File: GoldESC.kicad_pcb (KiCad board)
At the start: 4 copper layers, 98 x 40 mm, 153 parts, among them J1 PhaseOut, J10 Conn_01x06, J2 PhaseOut, J3 PhaseOut, J30 CanOut, J40 Supply, J81 Conn_02x07_Counter_Clockwise, J82 Conn_01x06, Q1 YJG150N03A, Q2 YJG150N03A, Q3 YJG150N03A, Q4 YJG150N03A, Q5 YJG150N03A, Q6 YJG150N03A, U2 DRV8300NIPWR, U30 MCP2551-I-SN, U31 CPDT-12V, U4 INA185A1, U5 INA185A1, U50 SY8113BADC, U6 INA185A1, U60 SY8113BADC, U80 STM32F103C8Tx, U81 Crystal_GND3

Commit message: major schematic and pcb changes for production ready prototype
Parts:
- removed ? (x3): , 
- removed C85: 2.2uF, Capacitor_SMD:C_0603_1608Metric
- removed D74, D75, D76, D77: Z3V3, Diode_SMD:D_MiniMELF
- removed D80, D81: LED_Dual_AKA, LED_THT:LED_D3.0mm-3
- removed J10: Conn_01x06, Connector_PinSocket_2.54mm:PinSocket_1x06_P2.54mm_Vertical
- removed L30: KCZ1210, AlfredoFootprints:KCZ1210
- removed R33: 120R?, Resistor_THT:R_Axial_DIN0207_L6.3mm_D2.5mm_P10.16mm_Horizontal
- removed R5, R6, R8, R9: 1K, Resistor_SMD:R_0603_1608Metric
- removed R77: 2K2, Resistor_SMD:R_0603_1608Metric
- removed TP1, TP10, TP11, TP12, TP13, TP14, TP15, TP2, TP3, TP30, TP31, TP32, TP33, TP4, TP40, TP41, TP5, TP50, TP6, TP7, TP8, TP81, TP9: TestPoint, AlfredoFootprints:GE_TestPoint_Loop
- removed the U50 at (175.4, 86.1)
- added C41: 330uF, AlfredoFootprints:Cap_THT_LowESR_330uF, B.Cu at (4.06, -4.19)
- added D82: LED_Green, LED_SMD:LED_0805_2012Metric, F.Cu at (6.60, 7.80)
- added D83: LED_Red, LED_SMD:LED_0805_2012Metric, F.Cu at (6.60, 6.20)
- added D84: LED_Green, LED_SMD:LED_0805_2012Metric, F.Cu at (6.60, -6.20)
- added D85: LED_Red, LED_SMD:LED_0805_2012Metric, F.Cu at (6.60, -7.80)
- added J4: GND, AlfredoFootprints:GE_PwrPad1, F.Cu at (22.2, 3.50)
- added J41: Gnd, AlfredoFootprints:GE_PwrPad1, F.Cu at (-0.45, -7.00)
- added J5: DB15_Female_HighDensity, Connector_Dsub:DSUB-15-HD_Female_Horizontal_P2.29x1.98mm_EdgePinOffset3.03mm_Housed_MountingHolesOffset4.94mm, F.Cu at (-130.5, -12.1)
- added REF**: MountingHole_2.2mm_M2, MountingHole:MountingHole_2.2mm_M2, F.Cu at (-23.4, 3.70)
- added REF**: MountingHole_2.2mm_M2, MountingHole:MountingHole_2.2mm_M2, F.Cu at (26.8, -3.43)
- added TP60: TestPoint, AlfredoFootprints:GE_TestPoint_Loop, F.Cu at (5.10, 14.3)
- added U50: SY8113BADC, Package_TO_SOT_SMD:TSOT-23-6, F.Cu at (-123.1, 34.7)
- added U50: SPX3819M5-L-3-3, Package_TO_SOT_SMD:SOT-23-5, F.Cu at (1.15, 15.2)
- C1, C2, C3: value 10uF,25V -> 2.2uF,50V; footprint Capacitor_SMD:C_0805_2012Metric -> Capacitor_SMD:C_1206_3216Metric
- C4, C42, C5, C50, C51, C52, C53, C6, C60, C61, C62, C63, C7, C8, C81, C82, C83, C84, C9: footprint Capacitor_SMD:C_0603_1608Metric -> Capacitor_SMD:C_0402_1005Metric
- C40: footprint AlfredoFootprints:TGD_lowESR_cap -> AlfredoFootprints:Cap_THT_LowESR_330uF; moved to B.Cu
- C80, C88, C89: footprint Capacitor_SMD:C_0603_1608Metric -> Capacitor_SMD:C_0402_1005Metric; moved to B.Cu
- D1, D2, D3, D42: value ZMM3V3 -> B3V3; footprint Diode_SMD:D_MiniMELF -> Diode_SMD:D_SOD-323_HandSoldering
- D4, D5, D6: value CRH01 -> 1N58; footprint Diode_SMD:D_SOD-123F -> Diode_SMD:D_SOD-323_HandSoldering
- D40, D41: value B5819W -> 1N58; footprint Diode_SMD:D_SOD-123 -> Diode_SMD:D_SOD-323_HandSoldering
- D70, D71, D72, D73: value Z3V3 -> SM05T1G; footprint Diode_SMD:D_MiniMELF -> Package_TO_SOT_SMD:SOT-23; moved to B.Cu
- G***: moved to F.Cu
- J1, J2, J3: footprint AlfredoFootprints:TGD_ESC_PwrPad -> AlfredoFootprints:GE_PwrPad1
- J40: value Supply -> Vin; footprint TerminalBlock:TerminalBlock_bornier-2_P5.08mm -> AlfredoFootprints:GE_PwrPad1
- J81: footprint Connector_IDC:IDC-Header_2x07_P2.54mm_Vertical -> AlfredoFootprints:Connector_2x05_P1.27mm_IDC
- J82: value Conn_01x06 -> Conn_01x04; footprint Connector_PinSocket_2.54mm:PinSocket_1x06_P2.54mm_Vertical -> AlfredoFootprints:Connector_1x04_P1.27mm_SwdProg
- Q1, Q2, Q3, U30, U31: moved to B.Cu
- R10, R11, R12, R13, R14, R15, R16, R17, R18, R19, R20, R21, R22, R23, R24, R40, R42, R43, R50, R51, R60, R61, R70, R71, R72, R73, R74, R75, R76, R80: footprint Resistor_SMD:R_0603_1608Metric -> Resistor_SMD:R_0402_1005Metric
- R30, R31, R4, R7, R81, R82, R83, R84, R85, R86: footprint Resistor_SMD:R_0603_1608Metric -> Resistor_SMD:R_0402_1005Metric; moved to B.Cu
- R32: value 50K? -> 50K; footprint Resistor_THT:R_Axial_DIN0207_L6.3mm_D2.5mm_P10.16mm_Horizontal -> Resistor_SMD:R_0402_1005Metric; moved to B.Cu
- R41: value 10K RTC -> 10K NTC; footprint Resistor_SMD:R_0603_1608Metric -> Resistor_SMD:R_0402_1005Metric
- U80: value STM32F103C8Tx -> STM32F103CBTx
- U81: value Crystal_GND3 -> ABM3B-8.000MHZ; moved to B.Cu
- moved R50 307.4 mm to (-123.7, 38.2), turned to 0 degrees
- moved R51 301.3 mm to (-118.1, 32.3), turned to 0 degrees
- moved R60 301.1 mm to (-114.1, 30.3), turned to 0 degrees
- moved U60 300.6 mm to (-117.5, 26.3), turned to 0 degrees
- moved C62 300.4 mm to (-118.5, 34.8), turned to 0 degrees
- moved L60 300.4 mm to (-122.9, 30.4), turned to 0 degrees
- moved D41 300.0 mm to (-114.0, 37.5)
- moved L50 299.4 mm to (-122.9, 26.1), turned to 0 degrees
- moved C52 299.4 mm to (-118.1, 29.8), turned to 0 degrees
- moved C61 297.5 mm to (-119.7, 38.2), turned to 0 degrees
- moved R61 294.9 mm to (-108.9, 27.8), turned to 0 degrees
- moved C60 294.8 mm to (-108.9, 25.3), turned to 0 degrees
- moved C63 293.8 mm to (-114.1, 32.8), turned to 0 degrees
- moved C53 292.0 mm to (-112.9, 27.8), turned to 0 degrees
- moved C51 291.9 mm to (-112.9, 25.3), turned to 0 degrees
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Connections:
- D70 pad 2: GND -> QuadA
- D71 pad 1: QuadA -> LimitA
- D71 pad 2: GND -> LimitB
- D72 pad 1: Limit2C -> LimitC
- D72 pad 2: GND -> LimitD
- D73 pad 1: Limit2A -> LimitE
- D73 pad 2: GND -> unconnected-(D73-Pad2)
- J40 pad 1: GND -> VDD
- J81 pad 1: +5V -> +3V3
- J81 pad 10: Limit1B -> LimitD
- J81 pad 2: QuadA -> +5V
- J81 pad 3: +3V3 -> GND
- J81 pad 4: QuadB -> LimitA
- J81 pad 5: GND -> QuadB_USBDM
- J81 pad 6: USB_DP -> LimitB
- J81 pad 7: GND -> QuadA_USBDP
- J81 pad 8: USB_DM -> LimitC
- J81 pad 9: Limit1C -> LimitE
- R4 pad 2: Net-(R4-Pad2) -> /GE-Fets-A/REF_1V65
- R7 pad 1: Net-(R4-Pad2) -> /GE-Fets-A/REF_1V65
- R72 pad 1: Limit2C -> LimitA
- R73 pad 1: Limit2A -> LimitB
- R74 pad 1: Limit1C -> LimitC
- R75 pad 1: Limit1A -> LimitD
- R76 pad 1: Limit1B -> LimitE
- R81 pad 2: USB_DM -> QuadB_USBDM
- R82 pad 2: USB_DP -> QuadA_USBDP
- U30 pad 6: Net-(L30-Pad2) -> CAN_L
- U30 pad 7: Net-(L30-Pad1) -> CAN_H
- U4 pad 5: Net-(R4-Pad2) -> /GE-Fets-A/REF_1V65
- U5 pad 5: Net-(R5-Pad2) -> /GE-Fets-A/REF_1V65
- U6 pad 5: Net-(R6-Pad2) -> /GE-Fets-A/REF_1V65
- U80 pad 17: QuadA -> unconnected-(U80-Pad17)
- U80 pad 19: QuadB -> unconnected-(U80-Pad19)
- U80 pad 38: Limit2C -> unconnected-(U80-Pad38)
- U80 pad 39: Limit1A -> LimitA
- U80 pad 40: Limit1B -> LimitB
- U80 pad 41: Limit1C -> LimitC
- U80 pad 42: Limit2A -> LimitD
- U80 pad 43: Limit2B -> LimitE
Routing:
- net VDD: track 158.0 -> 0.00 mm
- net GND: track 156.2 -> 0.00 mm, vias 41 -> 0
- net +5V: track 103.0 -> 0.00 mm, vias 6 -> 0
- net sVLT_B: track 95.8 -> 0.00 mm, vias 1 -> 0
- net sCUR_A: track 92.7 -> 0.00 mm, vias 1 -> 0
- net sCUR_B: track 92.5 -> 0.00 mm, vias 1 -> 0
- net sVLT_C: track 92.5 -> 0.00 mm, vias 1 -> 0
- net sVLT_A: track 88.8 -> 0.00 mm, vias 1 -> 0
- net sVLT_VDD: track 87.4 -> 0.00 mm, vias 1 -> 0
- net sCUR_C: track 87.3 -> 0.00 mm, vias 1 -> 0
- net INLC: track 67.2 -> 0.00 mm, vias 2 -> 0
- net /GE-Fets-B/SHx: track 63.5 -> 0.00 mm, vias 18 -> 0
- net TEMP_FETS: track 61.9 -> 0.00 mm, vias 1 -> 0
- net /GE-Fets-C/SHx: track 61.8 -> 0.00 mm, vias 16 -> 0
- net +3V3: track 56.8 -> 0.00 mm, vias 19 -> 0
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- removed copper zone on In2.Cu, net +3V3
- removed copper zone on B.Cu, net /GE-Fets-A/SHx
- removed copper zone on F.Cu, net /GE-Fets-A/SHx
- removed copper zone on B.Cu, net /GE-Fets-B/SHx
- removed copper zone on F.Cu, net /GE-Fets-B/SHx
- removed copper zone on B.Cu, net /GE-Fets-C/SHx
- removed copper zone on F.Cu, net /GE-Fets-C/SHx
- removed copper zone on B.Cu, net GND
- removed copper zone on In1.Cu, net GND
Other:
- board outline removed
- board text removed: "3V3"
- board text removed: "5V"
- board text removed: "A"
- board text removed: "B"
- board text removed: "C"
- board text removed: "CanH"
- board text removed: "CanL"
- board text removed: "GND"
- board text removed: "GoldESC V1 © Alfredo Systems 2022"
- board text removed: "HA"
- board text removed: "HB"
- board text removed: "HC"
- board text removed: "LA"
- board text removed: "LB"
- board text removed: "LC"
- board text removed: "SWCLK"
- board text removed: "SWDIO"

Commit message: First rev of layout before routing
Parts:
- removed C50: 10uF, Capacitor_SMD:C_0402_1005Metric
- removed C51: 100nF, Capacitor_SMD:C_0402_1005Metric
- removed D40, D41: 1N58, Diode_SMD:D_SOD-323_HandSoldering
- removed G***: LOGO, AlfredoFootprints:Alfredo_logo_small
- removed L50: 4.7uH, Inductor_SMD:L_1210_3225Metric
- removed R50: 100K, Resistor_SMD:R_0402_1005Metric
- removed R51: 22K, Resistor_SMD:R_0402_1005Metric
- removed R70, R71, R72, R73, R74, R75, R76: 2K2, Resistor_SMD:R_0402_1005Metric
- removed REF** (x2): MountingHole_2.2mm_M2, MountingHole:MountingHole_2.2mm_M2
- removed the U50 at (-123.1, 34.7)
- added D74: SD05, Diode_SMD:D_SOD-323, F.Cu at (-92.3, -4.77)
- added D75: SD05, Diode_SMD:D_SOD-323, F.Cu at (-76.4, -22.3)
- added D76: SD05, Diode_SMD:D_SOD-323, F.Cu at (-76.4, -19.4)
- C1, C2, C3: value 2.2uF,50V -> 4.7uF,50V; moved to B.Cu
- C10: value 1uF -> 10uF,50V; footprint Capacitor_SMD:C_0805_2012Metric -> Capacitor_SMD:C_1206_3216Metric
- C52: value 22pF -> 10nF, 6.3V; moved to B.Cu
- C53: value 22uF -> 2.2uF, 6.3V; moved to B.Cu
- C60: value 10uF -> 2.2uF, 50V; footprint Capacitor_SMD:C_0402_1005Metric -> Capacitor_SMD:C_0603_1608Metric; moved to B.Cu
- C61, C62, R60, R61, R80, TP60, U50, U60: moved to B.Cu
- C63: value 22uF -> 22uF, 10V; moved to B.Cu
- C88, C89, R32: moved to F.Cu
- D1, D2, D3, D42: value B3V3 -> Z3V3
- D4, D5, D6: value 1N58 -> SDM20U40-7; footprint Diode_SMD:D_SOD-323_HandSoldering -> Diode_SMD:D_SOD-523
- D70, D71, D72, D73: value SM05T1G -> SD05; footprint Package_TO_SOT_SMD:SOT-23 -> Diode_SMD:D_SOD-323; moved to F.Cu
- J30: footprint AlfredoFootprints:TGD_ESC_SigPads -> AlfredoFootprints:GE_SigPad_1x02
- R19, R20, R21: value 15R -> 2.2R
- R22, R23, R24: value 15R -> 0R
- R4: value 1K -> 2K
- R40: value 10K -> 20K
- U2: value DRV8300NIPWR -> FD8288T (DRV8300)
- moved L60 108.2 mm to (-18.4, 2.16), turned to 90 degrees
- moved C52 107.8 mm to (-12.5, 8.00)
- moved C61 107.0 mm to (-18.9, 2.20)
- moved C62 104.8 mm to (-17.7, 6.40)
- moved U60 102.0 mm to (-17.9, 4.40), turned to 180 degrees
- moved C63 101.9 mm to (-16.9, 2.20)
- moved C53 100.6 mm to (-14.3, 8.00), turned to 180 degrees
- moved R60 99.1 mm to (-17.7, 7.30), turned to 180 degrees
- moved R61 93.3 mm to (-17.7, 8.20)
- moved C60 91.5 mm to (-19.2, 7.30), turned to 90 degrees
- moved D71 90.6 mm to (-109.3, -4.77), turned to 0 degrees
- moved D72 85.8 mm to (-105.1, -4.77), turned to 0 degrees
- moved D70 81.6 mm to (-100.8, -4.77), turned to 0 degrees
- moved D73 77.6 mm to (-96.6, -4.77), turned to 0 degrees
- moved J5 40.7 mm to (-90.7, -20.7), turned to 0 degrees
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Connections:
- C10 pad 1: VDD -> +5V
- C52 pad 1: Net-(C52-Pad1) -> GND
- C52 pad 2: +3V3 -> Net-(C52-Pad2)
- D4 pad 2: VDD -> +5V
- D5 pad 2: VDD -> +5V
- D6 pad 2: VDD -> +5V
- D70 pad 1: QuadB -> unconnected-(D70-Pad1)
- D70 pad 2: QuadA -> unconnected-(D70-Pad2)
- D71 pad 1: LimitA -> unconnected-(D71-Pad1)
- D71 pad 2: LimitB -> unconnected-(D71-Pad2)
- D72 pad 1: LimitC -> unconnected-(D72-Pad1)
- D72 pad 2: LimitD -> unconnected-(D72-Pad2)
- D73 pad 1: LimitE -> unconnected-(D73-Pad1)
- R4 pad 1: +3V3 -> +5V
- R40 pad 1: TEMP_FETS -> +5V
- R40 pad 2: GND -> TEMP_FETS
- R41 pad 1: +3V3 -> TEMP_FETS
- R41 pad 2: TEMP_FETS -> GND
- U2 pad 7: VDD -> +5V
- U4 pad 6: +3V3 -> +5V
- U5 pad 6: +3V3 -> +5V
- U50 pad 4: unconnected-(U50-Pad4) -> Net-(C52-Pad2)
- U6 pad 6: +3V3 -> +5V
- U80 pad 26: INLA -> INLC
- U80 pad 28: INLC -> INLA
- U80 pad 29: INHA -> INHC
- U80 pad 31: INHC -> INHA
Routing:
- net VDD: track 0.00 -> 12.6 mm
- net /GE-Fets-C/SHx: track 0.00 -> 11.6 mm
- net GND: track 0.00 -> 7.70 mm
- net Net-(J3-Pad1): track 0.00 -> 5.94 mm
- net Net-(R18-Pad2): track 0.00 -> 3.40 mm
- net Net-(Q3-Pad4): track 0.00 -> 1.75 mm, vias 0 -> 1
- net sCUR_C: track 0.00 -> 1.51 mm, vias 0 -> 1
- net Net-(Q6-Pad4): track 0.00 -> 1.45 mm, vias 0 -> 1
- net sVLT_C: track 0.00 -> 1.39 mm
- net Net-(Q4-Pad4): track 0.00 -> 0.94 mm, vias 0 -> 1
- net Net-(Q5-Pad4): track 0.00 -> 0.84 mm, vias 0 -> 1
- net +5V: track 0.00 -> 0.83 mm, vias 0 -> 1
- net /GE-Fets-A/REF_1V65: track 0.00 -> 0.65 mm, vias 0 -> 1
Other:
- board outline added: 45 x 17.4 mm
- board text added: "A"

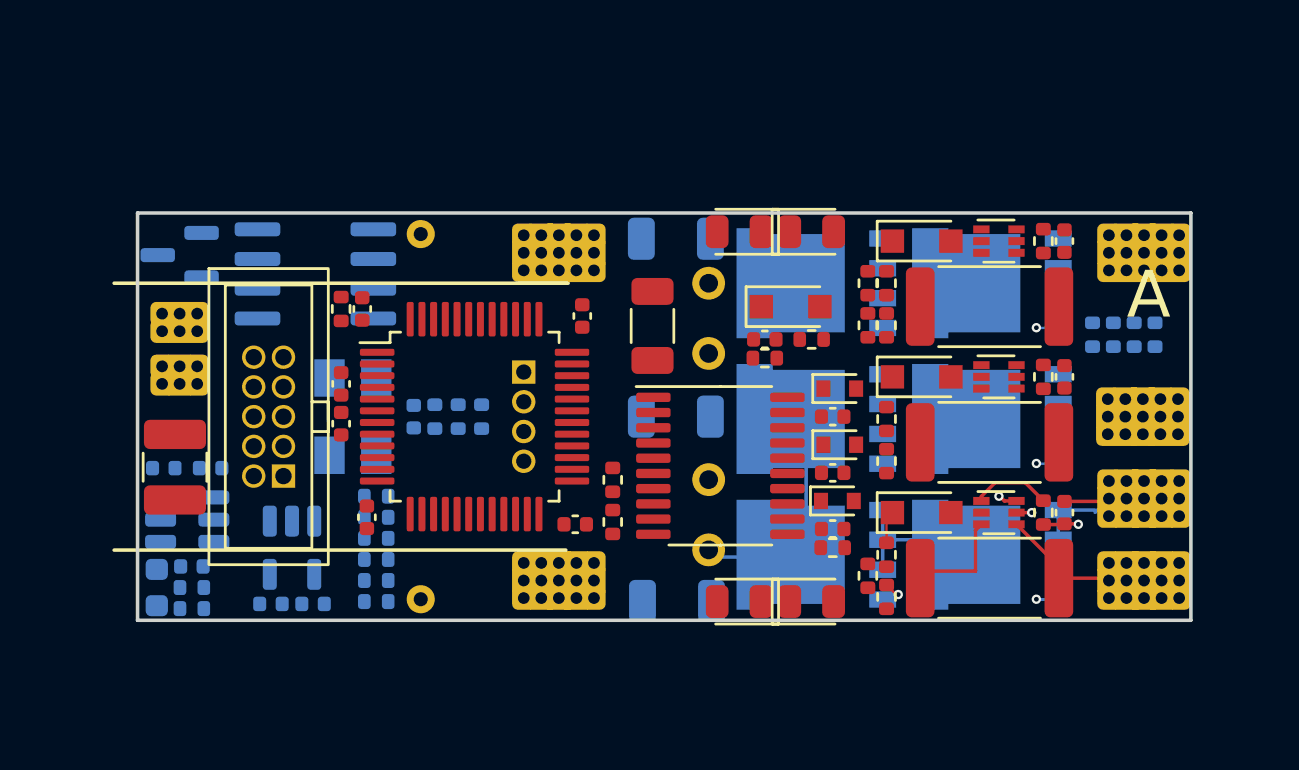
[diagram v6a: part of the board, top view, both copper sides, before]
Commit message: all nets routed for next revision, no major drc errors
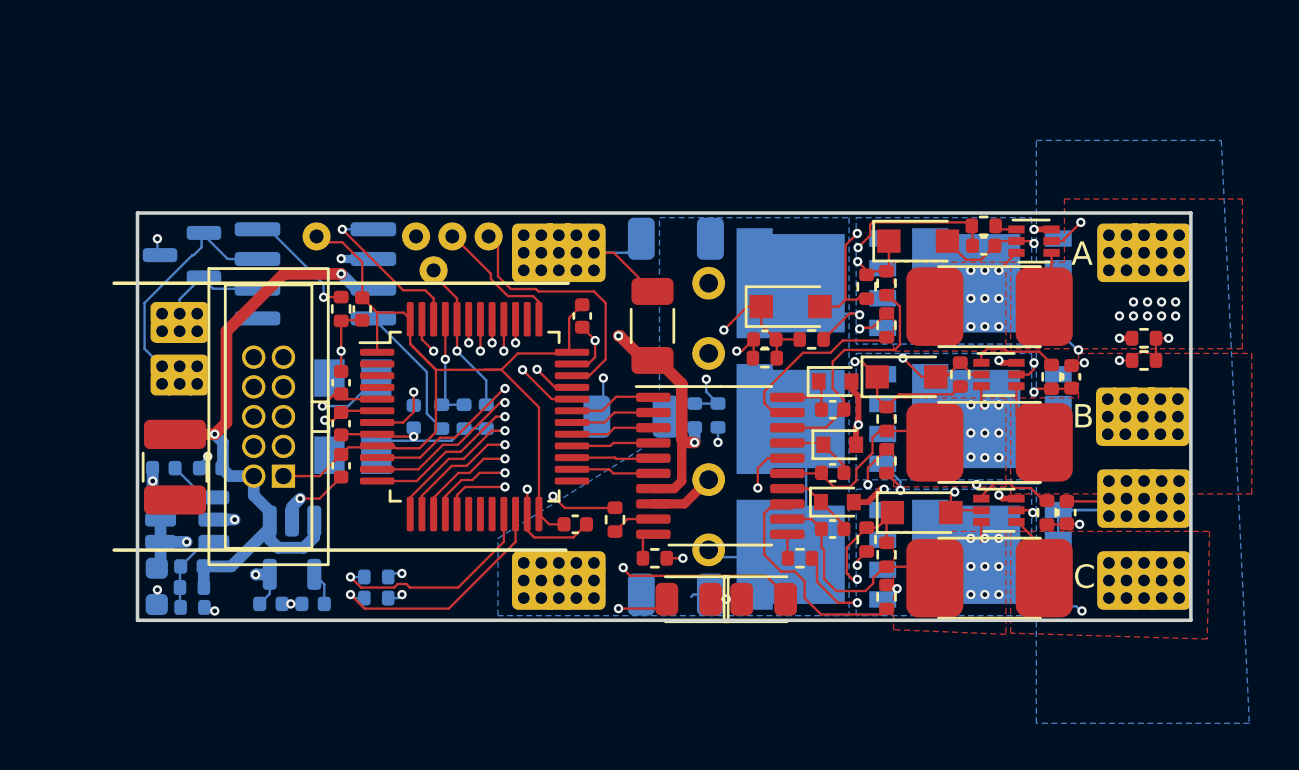
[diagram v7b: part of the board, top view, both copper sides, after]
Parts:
- removed D82: LED_Green, LED_SMD:LED_0805_2012Metric
- removed D85: LED_Red, LED_SMD:LED_0805_2012Metric
- removed J82: Conn_01x04, AlfredoFootprints:Connector_1x04_P1.27mm_SwdProg
- removed R81, R82: 22R, Resistor_SMD:R_0402_1005Metric
- removed R83, R86: 200R, Resistor_SMD:R_0402_1005Metric
- removed TP60: TestPoint, AlfredoFootprints:GE_TestPoint_Loop
- added TP81: TestPoint, AlfredoFootprints:GE_TestPoint_Loop, F.Cu at (-6.55, -7.70)
- added TP82: TestPoint, AlfredoFootprints:GE_TestPoint_Loop, F.Cu at (-5.00, -7.70)
- added TP83: TestPoint, AlfredoFootprints:GE_TestPoint_Loop, F.Cu at (-12.3, -7.70)
- added TP84: TestPoint, AlfredoFootprints:GE_TestPoint_Loop, F.Cu at (-8.10, -7.70)
- R1, R2, R3: footprint Resistor_SMD:R_2512_6332Metric -> AlfredoFootprints:GE_R_2512
- R19, R20, R21: value 2.2R -> 10R
- R22, R23, R24: value 0R -> 10R
- R4, R7: moved to F.Cu
- moved R40 18.2 mm to (3.80, -0.05)
- moved R41 16.4 mm to (4.80, -0.05)
- moved D84 15.8 mm to (6.75, 7.80)
- moved D83 5.25 mm to (3.55, 7.80), turned to 180 degrees
- moved R14 4.47 mm to (15.2, -1.80)
- moved C7 3.46 mm to (16.1, -7.30), turned to 180 degrees
- moved R16 2.63 mm to (16.1, -8.15), turned to 0 degrees
- moved C84 2.46 mm to (-11.3, 2.10)
- moved R23 2.38 mm to (2.10, 6.05), turned to 180 degrees
- moved C2 1.90 mm to (1.10, 0.00)
- moved R24 1.70 mm to (0.40, 4.40)
- moved TP80 1.64 mm to (-7.35, -6.25)
- moved R15 1.55 mm to (11.2, 5.25)
- moved U4 1.50 mm to (18.3, -7.50)
- moved R22 1.47 mm to (8.30, 6.05)
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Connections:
- U80 pad 10: sVLT_VDD -> sCUR_A
- U80 pad 11: sCUR_A -> sVLT_A
- U80 pad 12: sCUR_B -> sVLT_VDD
- U80 pad 13: sCUR_C -> TEMP_FETS
- U80 pad 14: sVLT_A -> sVLT_B
- U80 pad 15: sVLT_B -> sCUR_B
- U80 pad 16: sVLT_C -> sCUR_C
- U80 pad 17: unconnected-(U80-Pad17) -> sVLT_C
- U80 pad 18: TEMP_FETS -> unconnected-(U80-Pad18)
- U80 pad 20: Net-(R83-Pad2) -> unconnected-(U80-Pad20)
- U80 pad 25: Net-(R86-Pad2) -> unconnected-(U80-Pad25)
- U80 pad 32: Net-(R81-Pad1) -> QuadB_USBDM
- U80 pad 33: Net-(R82-Pad1) -> QuadA_USBDP
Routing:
- net +5V: track 0.83 -> 108.2 mm, vias 1 -> 10
- net GND: track 7.70 -> 75.0 mm, vias 0 -> 33
- net +3V3: track 0.00 -> 46.3 mm, vias 0 -> 1
- net sCUR_A: track 0.00 -> 31.5 mm, vias 0 -> 2
- net sCUR_C: track 1.51 -> 32.5 mm, vias 1 -> 2
- net sCUR_B: track 0.00 -> 29.8 mm, vias 0 -> 2
- net sVLT_A: track 0.00 -> 27.9 mm, vias 0 -> 2
- net sVLT_B: track 0.00 -> 27.8 mm, vias 0 -> 2
- net Net-(Q6-Pad4): track 1.45 -> 28.8 mm, vias 1 -> 2
- net VDD: track 12.6 -> 39.3 mm, vias 0 -> 2
- net /GE-Fets-A/REF_1V65: track 0.65 -> 26.8 mm, vias 1 -> 4
- net sVLT_C: track 1.39 -> 25.7 mm, vias 0 -> 2
- net Net-(Q4-Pad4): track 0.94 -> 24.9 mm, vias 1 -> 2
- net sVLT_VDD: track 0.00 -> 23.7 mm, vias 0 -> 2
- net Net-(D84-Pad2): track 0.00 -> 21.0 mm, vias 0 -> 2
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- added copper zone on B.Cu, net /GE-Fets-A/SHx
- added copper zone on F.Cu, net /GE-Fets-A/SHx
- added copper zone on B.Cu, net /GE-Fets-B/SHx
- added copper zone on F.Cu, net /GE-Fets-B/SHx
- added copper zone on B.Cu, net /GE-Fets-C/SHx
- added copper zone on F.Cu, net /GE-Fets-C/SHx
- added copper zone on B.Cu, net GND
- added copper zone on In1.Cu, net GND
- added copper zone on F.Cu, net Net-(J1-Pad1)
- added copper zone on F.Cu, net Net-(J2-Pad1)
- added copper zone on F.Cu, net Net-(J3-Pad1)
- added copper zone on B.Cu, net VDD
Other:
- board text added: "B"
- board text added: "C"

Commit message: version for 9/10/22 jlc order
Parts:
- removed D70, D71, D72, D73, D74, D75, D76: SD05, Diode_SMD:D_SOD-323
- removed J5: DB15_Female_HighDensity, Connector_Dsub:DSUB-15-HD_Female_Horizontal_P2.29x1.98mm_EdgePinOffset3.03mm_Housed_MountingHolesOffset4.94mm
- R32: value 50K -> 51K
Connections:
- J81 pad 10: LimitD -> SWCLK
- J81 pad 9: LimitE -> SWDIO
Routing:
- net SWCLK: track 5.73 -> 21.3 mm
- net LimitD: track 12.1 -> 0.00 mm, vias 1 -> 0
- net SWDIO: track 11.1 -> 23.0 mm
- net LimitE: track 9.45 -> 0.00 mm, vias 1 -> 0
- net Net-(R32-Pad1): track 5.11 -> 5.87 mm
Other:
- board text added: "3V"
- board text added: "C,D"
- board text added: "G"
- board text added: "GND"
- board text added: "H"
- board text added: "L"
- board text added: "VIN"
